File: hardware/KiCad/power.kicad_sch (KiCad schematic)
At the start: 9 parts, among them U8 SCT2A25STER

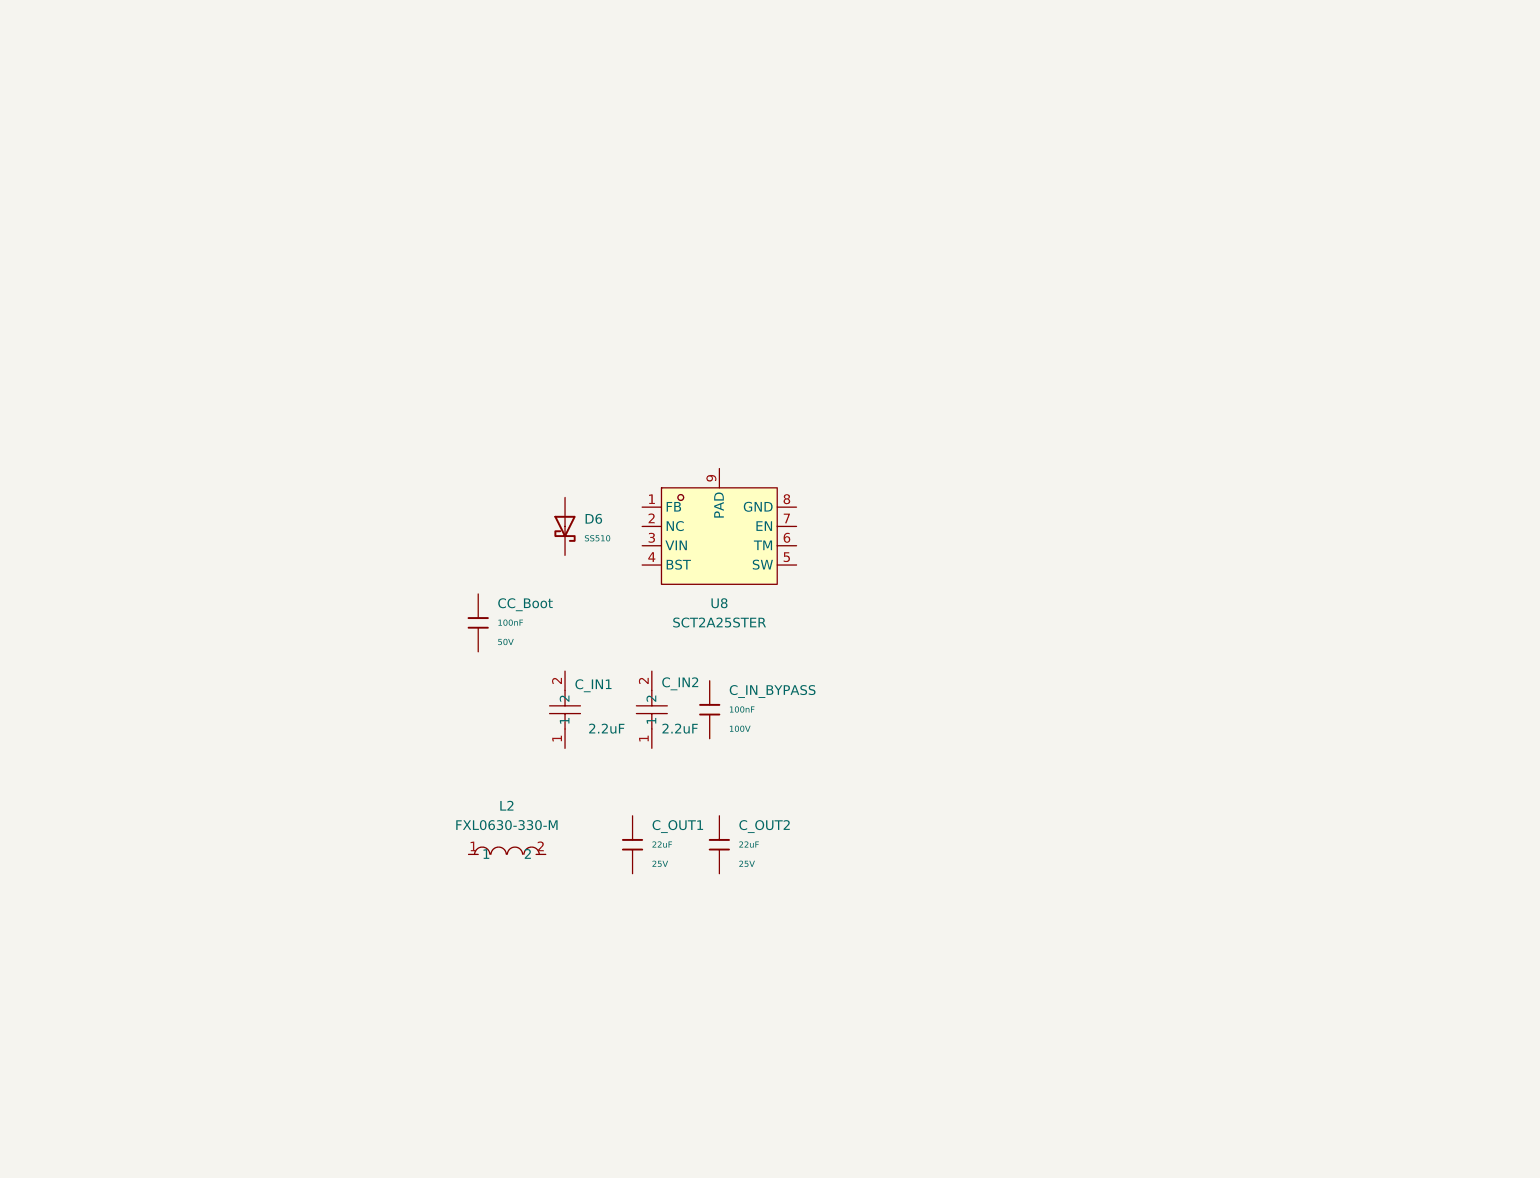
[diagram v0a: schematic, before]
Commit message: finished 10V regulator
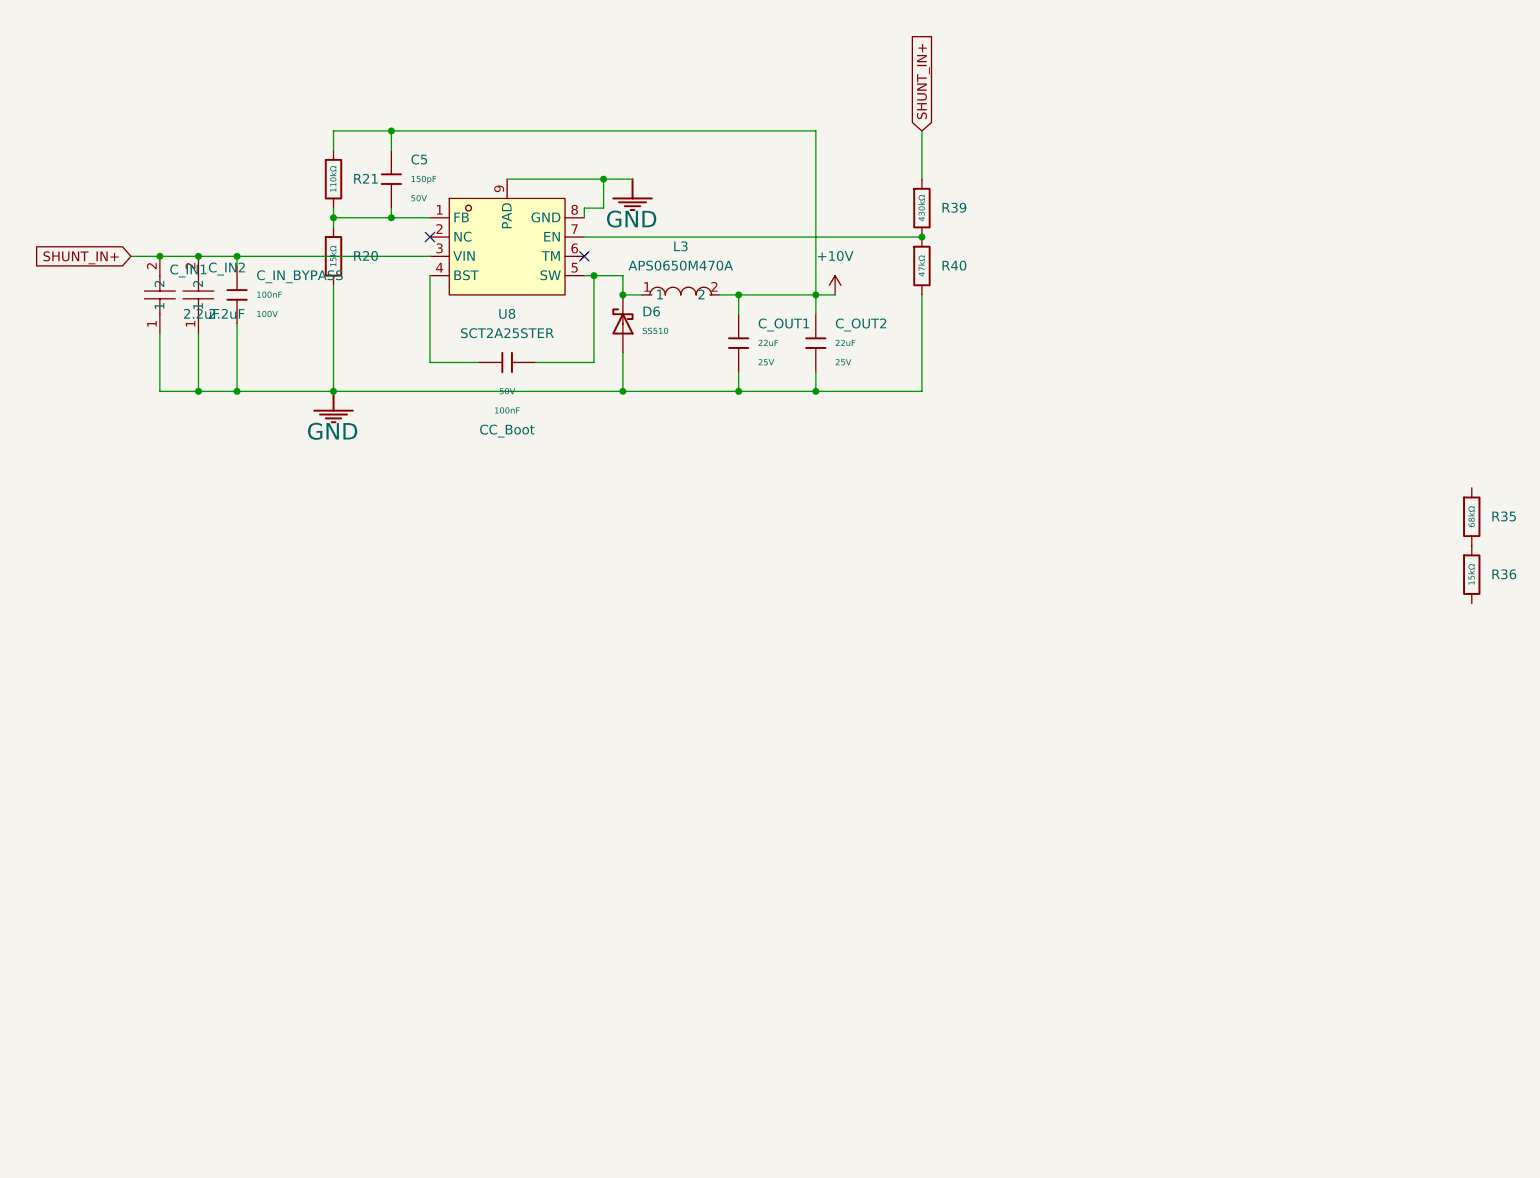
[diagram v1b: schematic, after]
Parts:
- removed L2: FXL0630-330-M, easyeda2kicad:IND-SMD_L7.0-W6.6_FXL0630, symbol easyeda2kicad:FXL0630-330-M
- added C5: 150pF, PCM_JLCPCB:C_0603, symbol JLCPCB-Capacitors:0603,150pF
- added L3: APS0650M470A, easyeda2kicad:IND-SMD_L7.7-W6.6_APS07A30M220, symbol easyeda2kicad:APS0650M470A
- added R20, R36: 15kΩ, PCM_JLCPCB:R_0603, symbol JLCPCB-Resistors:0603,15kΩ
- added R21: 110kΩ, PCM_JLCPCB:R_0603, symbol JLCPCB-Resistors:0603,110kΩ
- added R35: 68kΩ, PCM_JLCPCB:R_0603, symbol JLCPCB-Resistors:0603,68kΩ
- added R39: 430kΩ, PCM_JLCPCB:R_0603, symbol JLCPCB-Resistors:0603,430kΩ
- added R40: 47kΩ, PCM_JLCPCB:R_0603, symbol JLCPCB-Resistors:0603,47kΩ
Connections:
- net at CC_Boot.1: now also U8.4 (BST)
- net at CC_Boot.2: now also D6.1, U8.5 (SW), L3.1
- net GND: now reaches C_IN1.1
- net GND: now also C_IN2.1, C_IN_BYPASS.2, C_OUT1.2, C_OUT2.2, D6.2, U8.8 (GND), U8.9 (PAD), R20.2, R40.2
- net SHUNT_IN+: now reaches C_IN1.2
- net SHUNT_IN+: now also C_IN2.2, C_IN_BYPASS.1, U8.3 (VIN), R39.1
- net at U8.1 (FB): now also C5.2, R20.1, R21.2
- net at U8.7 (EN): now also R39.2, R40.1
- net +10V: now reaches C_OUT1.1
- net +10V: now also C_OUT2.1, C5.1, L3.2, R21.1
- new net: R35.2, R36.1
- no-connect marks 0 -> 2
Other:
- moved on the sheet: CC_Boot, C_IN1, C_IN2, C_IN_BYPASS, C_OUT1, C_OUT2, D6, U8

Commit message: added 3v3 regulator
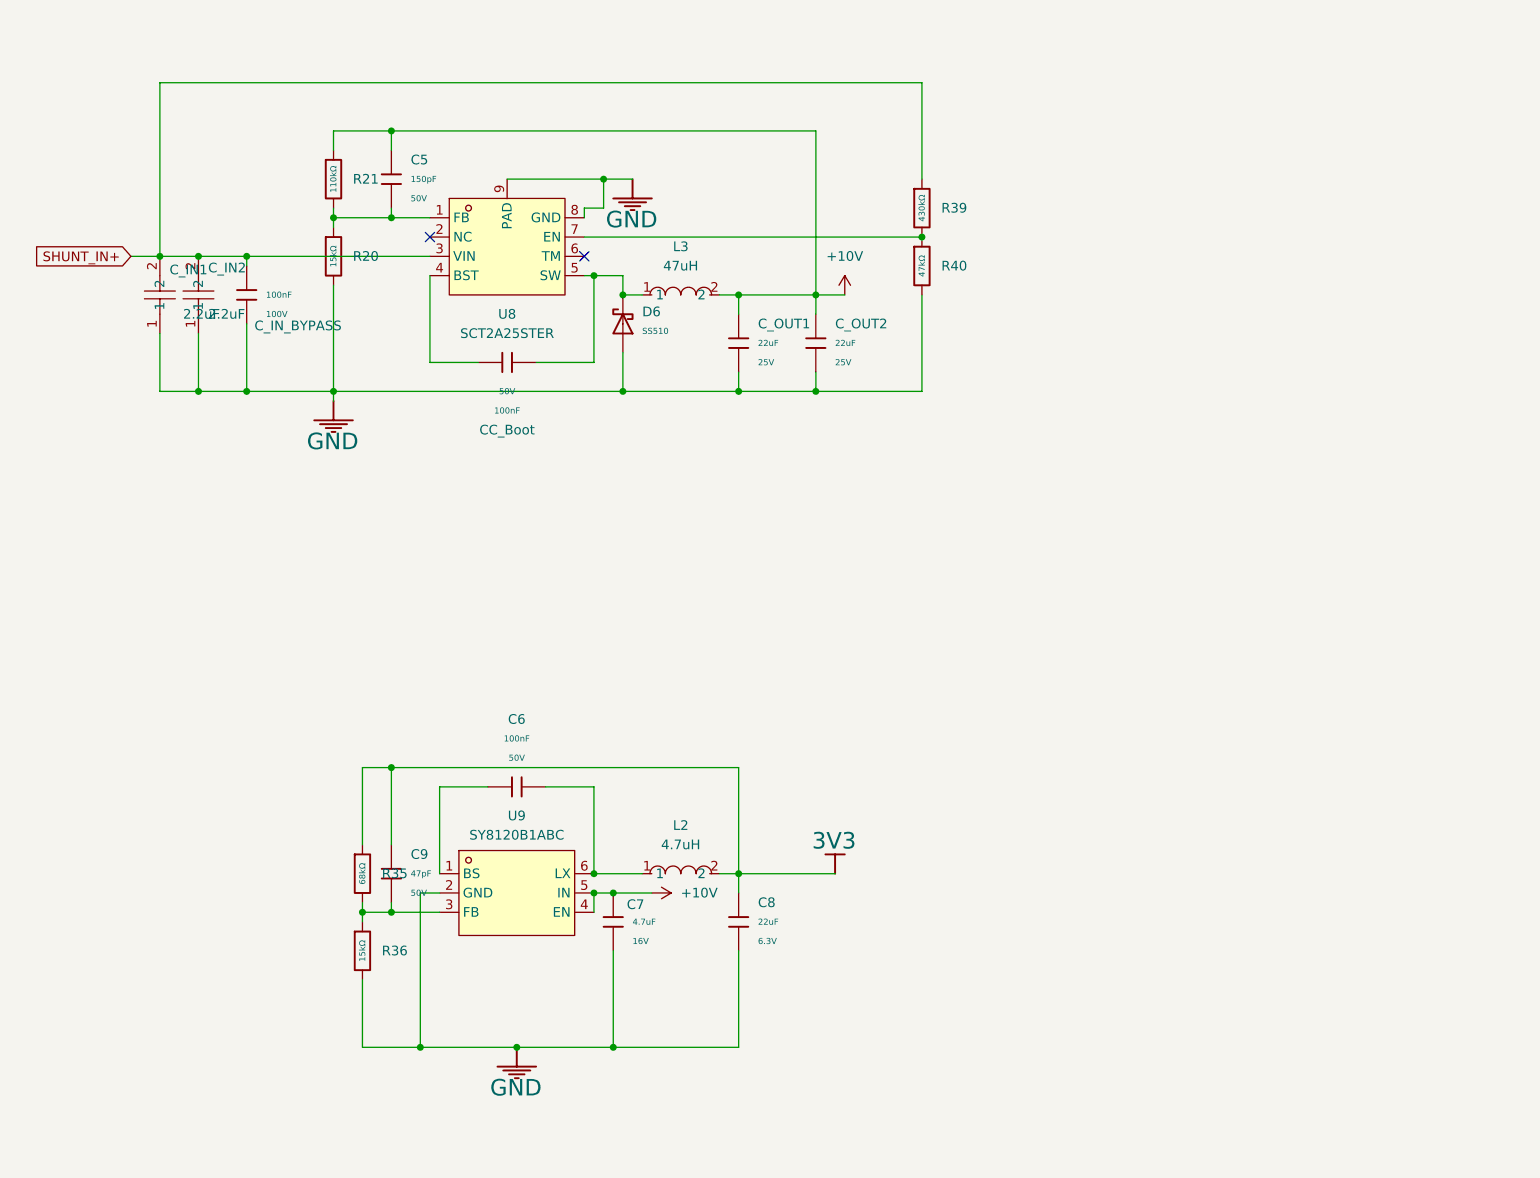
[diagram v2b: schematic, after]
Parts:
- added C6: 100nF, PCM_JLCPCB:C_0603, symbol JLCPCB-Capacitors:0603,100nF
- added C7: 4.7uF, PCM_JLCPCB:C_0603, symbol JLCPCB-Capacitors:0603,4.7uF
- added C8: 22uF, PCM_JLCPCB:C_0603, symbol JLCPCB-Capacitors:0603,22uF
- added C9: 47pF, PCM_JLCPCB:C_0603, symbol JLCPCB-Capacitors:0603,47pF
- added L2: 4.7uH, easyeda2kicad:IND-SMD_L2.0-W1.6-B, symbol easyeda2kicad:FTC201610S4R7MBCA
- added U9: SY8120B1ABC, easyeda2kicad:SOT-23-6_L2.9-W1.6-P0.95-LS2.8-BL, symbol easyeda2kicad:SY8120B1ABC
- L3: value APS0650M470A -> 47uH
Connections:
- net +10V: now also C7.1, U9.4 (EN), U9.5 (IN)
- net GND: now also R36.2, C7.2, C8.2, U9.2 (GND)
- net 3V3: now reaches R35.1
- net 3V3: now also C8.1, C9.1, L2.2
- net at R35.2, R36.1: now also C9.2, U9.3 (FB)
- new net: C6.2, L2.1, U9.6 (LX)
- new net: C6.1, U9.1 (BS)
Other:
- moved on the sheet: C_IN_BYPASS, R35, R36

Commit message: added hall effect
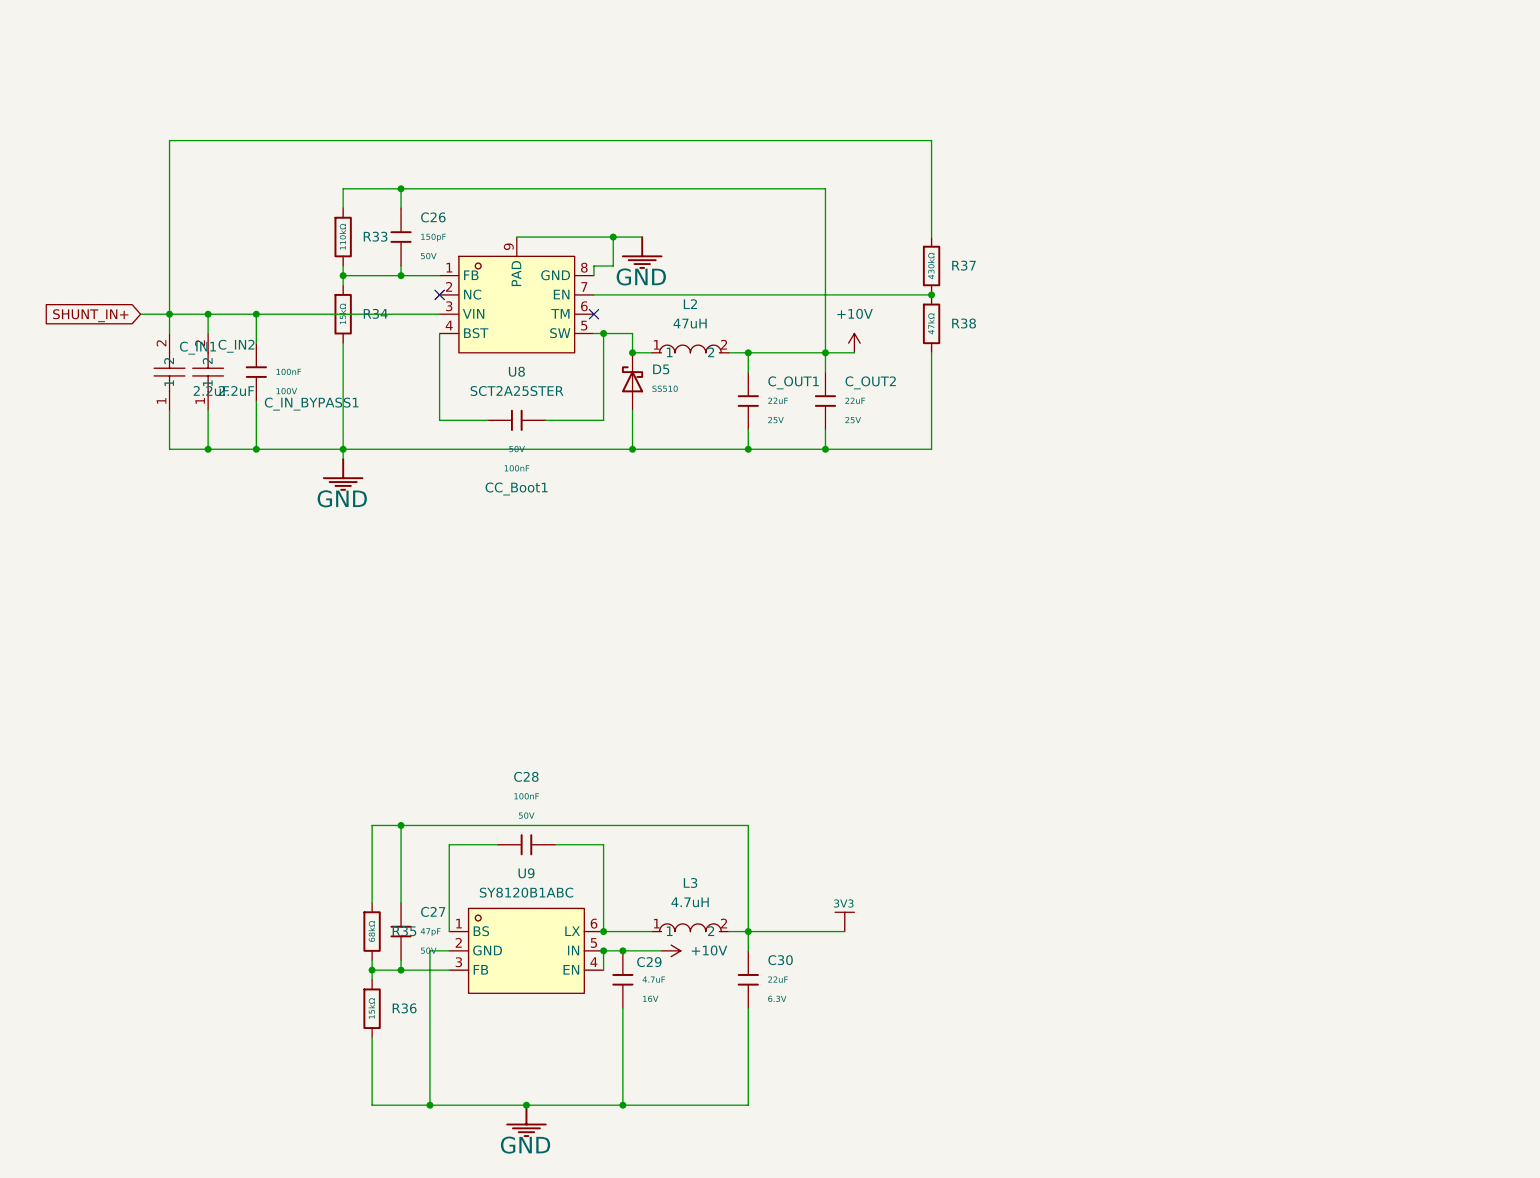
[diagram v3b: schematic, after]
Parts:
- removed C5: 150pF, PCM_JLCPCB:C_0603, symbol JLCPCB-Capacitors:0603,150pF
- removed C6, CC_Boot: 100nF, PCM_JLCPCB:C_0603, symbol JLCPCB-Capacitors:0603,100nF
- removed C7: 4.7uF, PCM_JLCPCB:C_0603, symbol JLCPCB-Capacitors:0603,4.7uF
- removed C8: 22uF, PCM_JLCPCB:C_0603, symbol JLCPCB-Capacitors:0603,22uF
- removed C9: 47pF, PCM_JLCPCB:C_0603, symbol JLCPCB-Capacitors:0603,47pF
- removed C_IN_BYPASS: 100nF, PCM_JLCPCB:C_0805, symbol JLCPCB-Capacitors:0805,100nF
- removed D6: SS510, PCM_JLCPCB:D_SMA, symbol JLCPCB-Diodes:Schottky,SS510
- removed L2: 4.7uH, easyeda2kicad:IND-SMD_L2.0-W1.6-B, symbol easyeda2kicad:FTC201610S4R7MBCA
- removed L3: 47uH, easyeda2kicad:IND-SMD_L7.7-W6.6_APS07A30M220, symbol easyeda2kicad:APS0650M470A
- removed R20: 15kΩ, PCM_JLCPCB:R_0603, symbol JLCPCB-Resistors:0603,15kΩ
- removed R21: 110kΩ, PCM_JLCPCB:R_0603, symbol JLCPCB-Resistors:0603,110kΩ
- removed R39: 430kΩ, PCM_JLCPCB:R_0603, symbol JLCPCB-Resistors:0603,430kΩ
- removed R40: 47kΩ, PCM_JLCPCB:R_0603, symbol JLCPCB-Resistors:0603,47kΩ
- added C26: 150pF, PCM_JLCPCB:C_0603, symbol JLCPCB-Capacitors:0603,150pF
- added C27: 47pF, PCM_JLCPCB:C_0603, symbol JLCPCB-Capacitors:0603,47pF
- added C28, CC_Boot1: 100nF, PCM_JLCPCB:C_0603, symbol JLCPCB-Capacitors:0603,100nF
- added C29: 4.7uF, PCM_JLCPCB:C_0603, symbol JLCPCB-Capacitors:0603,4.7uF
- added C30: 22uF, PCM_JLCPCB:C_0603, symbol JLCPCB-Capacitors:0603,22uF
- added C_IN_BYPASS1: 100nF, PCM_JLCPCB:C_0805, symbol JLCPCB-Capacitors:0805,100nF
- added D5: SS510, PCM_JLCPCB:D_SMA, symbol JLCPCB-Diodes:Schottky,SS510
- added L2: 47uH, easyeda2kicad:IND-SMD_L7.7-W6.6_APS07A30M220, symbol easyeda2kicad:APS0650M470A
- added L3: 4.7uH, easyeda2kicad:IND-SMD_L2.0-W1.6-B, symbol easyeda2kicad:FTC201610S4R7MBCA
- added R33: 110kΩ, PCM_JLCPCB:R_0603, symbol JLCPCB-Resistors:0603,110kΩ
- added R34: 15kΩ, PCM_JLCPCB:R_0603, symbol JLCPCB-Resistors:0603,15kΩ
- added R37: 430kΩ, PCM_JLCPCB:R_0603, symbol JLCPCB-Resistors:0603,430kΩ
- added R38: 47kΩ, PCM_JLCPCB:R_0603, symbol JLCPCB-Resistors:0603,47kΩ
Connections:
- net +10V: now also C26.1, C29.1, L2.2, R33.1
- net 3V3: now also C27.1, C30.1, L3.2
- net GND: now also C29.2, C30.2, C_IN_BYPASS1.2, D5.2, R34.2, R38.2
- net SHUNT_IN+: now also C_IN_BYPASS1.1, R37.1
- net at R35.2, R36.1, U9.3 (FB): now also C27.2
- net at U8.1 (FB): now also C26.2, R33.2, R34.1
- net at U9.6 (LX): now also C28.2, L3.1
- net at U8.4 (BST): now also CC_Boot1.1
- net at U8.5 (SW): now also CC_Boot1.2, D5.1, L2.1
- net at U8.7 (EN): now also R37.2, R38.1
- net at U9.1 (BS): now also C28.1

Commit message: updates
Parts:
- renumbered C26 to C32, C27 to C33, C28 to C34, C29 to C35, C30 to C36, D5 to D7, R33 to R30, R34 to R31, R35 to R32, R36 to R33, R37 to R34, R38 to R35, U8 to U4, U9 to U5
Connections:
- net GND: no longer R31.2

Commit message: changes
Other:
- moved on the sheet: C35, C36

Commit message: started layout
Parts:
- added D8: 12V, PCM_JLCPCB:DFN2020-3_L2.0-W2.0-P0.65-BR-1, symbol JLCPCB-Diode-Packages:TVS-Uni, H12VH22U
- added D9: 3.3V, PCM_JLCPCB:D_DFN0603-2L, symbol JLCPCB-Diodes:TVS-Bi,H3V3L06B
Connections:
- net +10V: now also D8.3 (K)
- net 3V3: now also D9.2
- net GND: now also D8.1 (A), D8.2 (A), D9.1
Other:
- moved on the sheet: R34, R35
